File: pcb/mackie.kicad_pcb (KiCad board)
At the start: 2 copper layers, 50 x 50 mm, 28 parts, among them J1 Conn_01x05, SW1 SW_PUSH, SW2 SW_PUSH, U1 STM32F072CBTx, U2 TLV75533PDBV

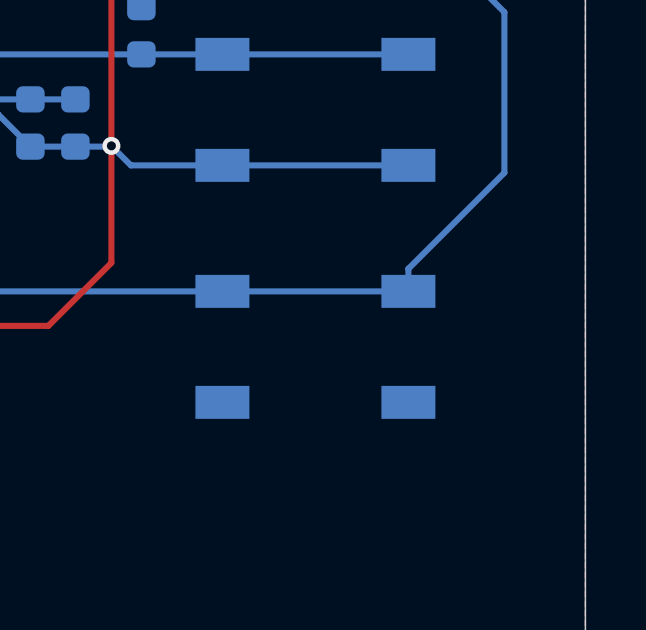
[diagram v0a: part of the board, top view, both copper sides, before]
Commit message: added debouncing cap
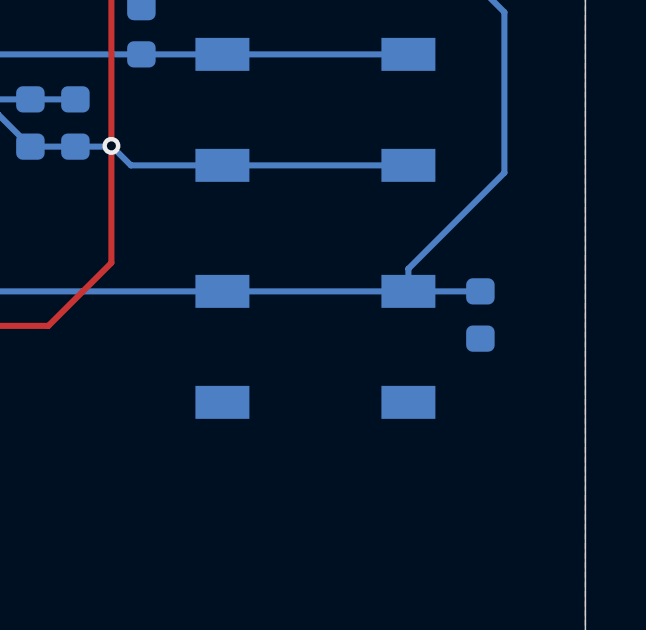
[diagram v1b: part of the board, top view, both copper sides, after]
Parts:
- added C10: 1uf, Capacitor_SMD:C_0603_1608Metric, B.Cu at (46.5, 39.4)
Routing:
- net NRST: track 41.0 -> 43.4 mm
